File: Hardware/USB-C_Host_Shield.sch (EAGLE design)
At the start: 39 parts, among them J1 USB-C, J2 GPIN, J3 GPOUT, U1 ARDUINO_UNO_R3_SHIELDBASIC, U2 LM1117, U3 74HC4050, U5 MAX3421, U6 3.3V/150mA, Y1 12.0mhZ

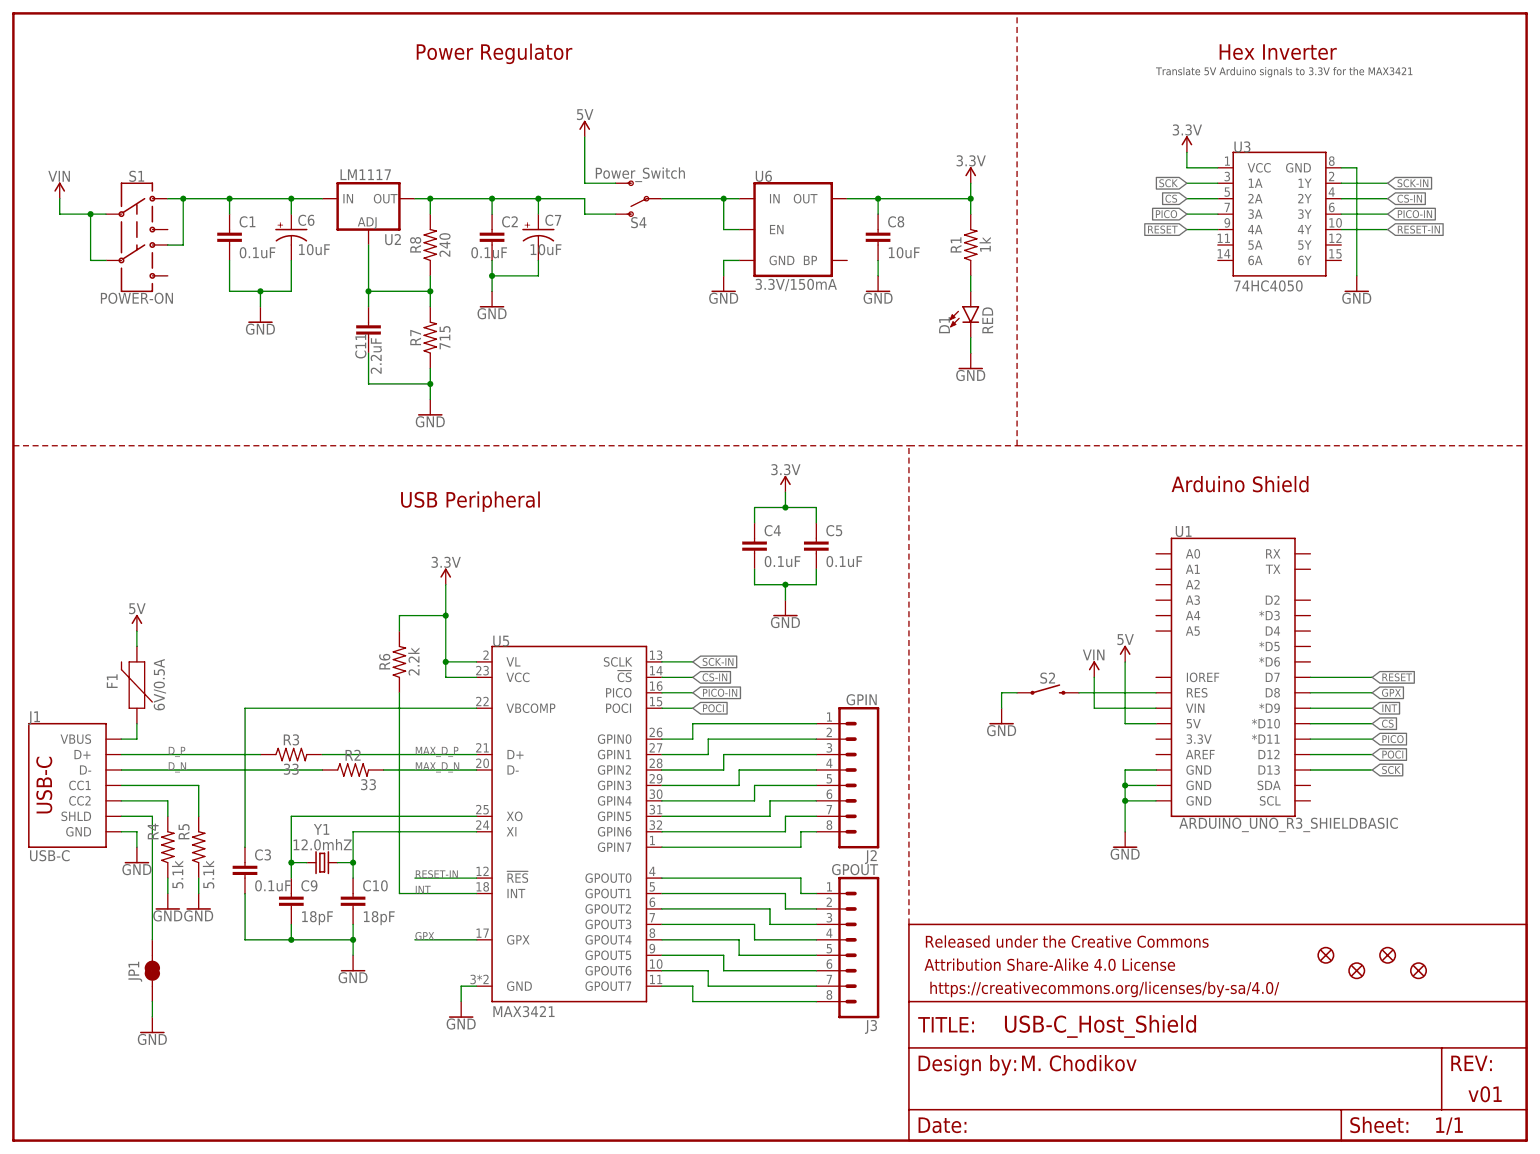
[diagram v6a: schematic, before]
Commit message: Updates from design review
Adjusted text in schematic to vector font, added pullup resistors to CC1 and CC2, changed power selection and power off section, added lines to silk screen GPIO pins
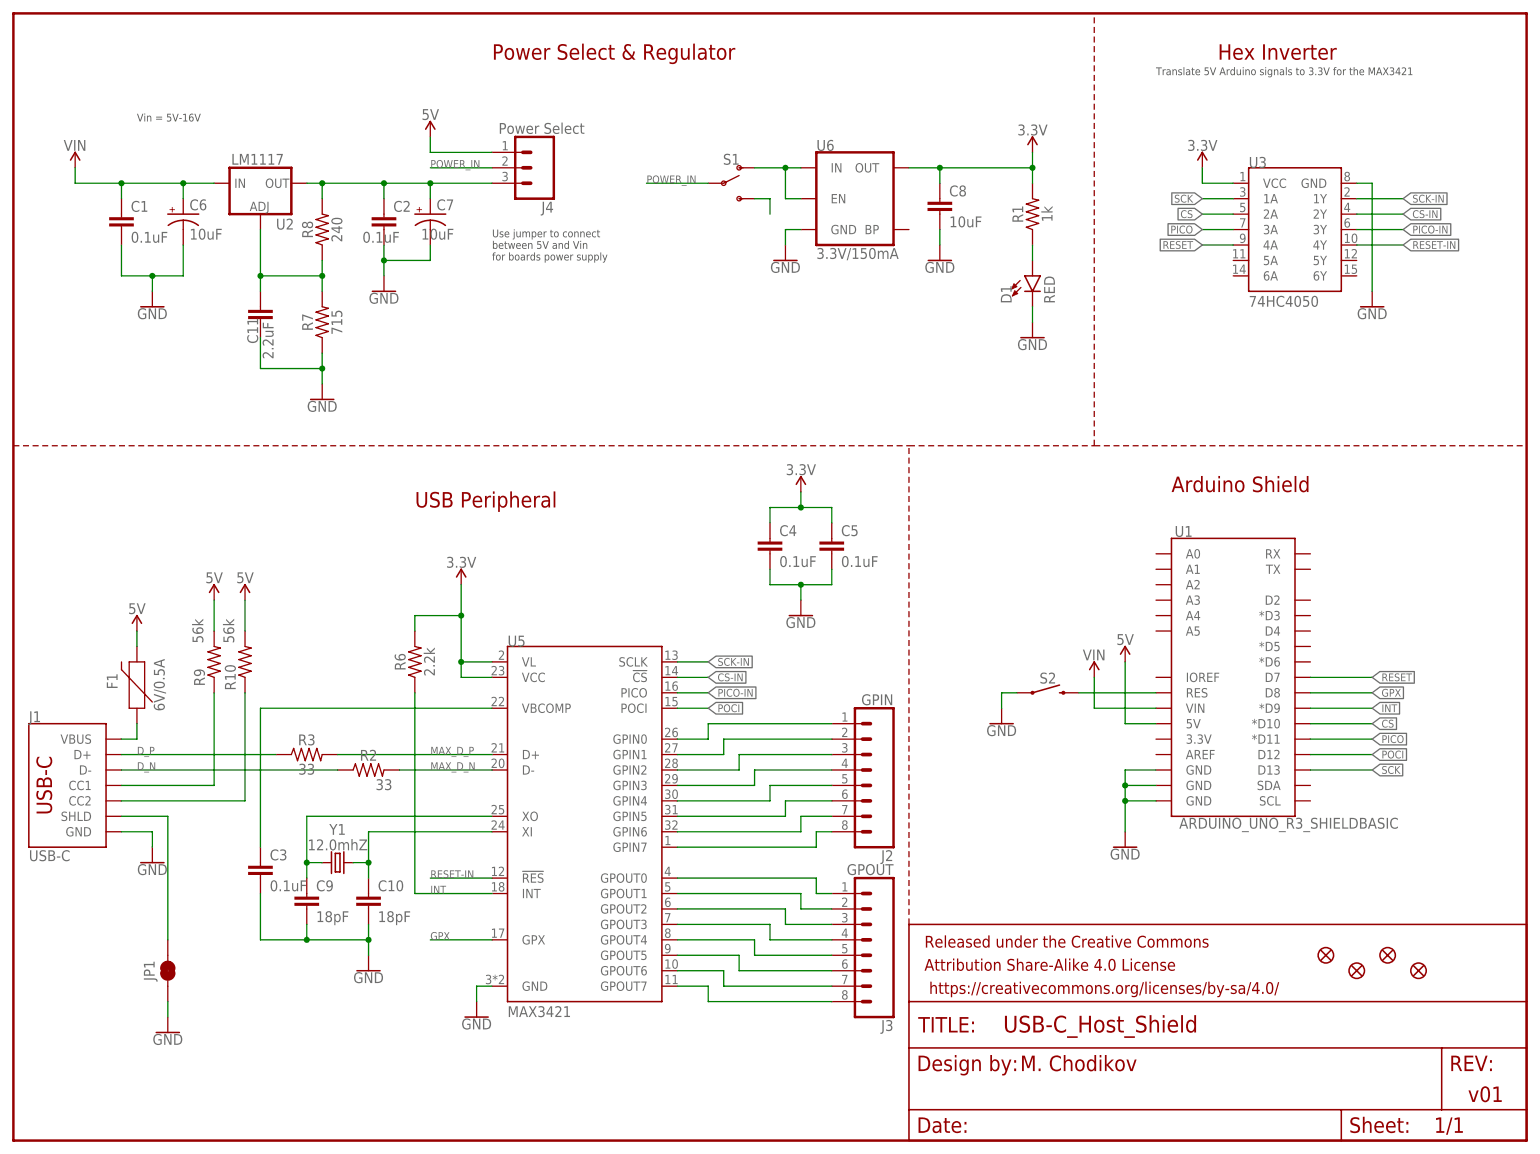
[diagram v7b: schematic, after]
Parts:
- removed R4, R5: 5.1k, SparkFun-Resistors:5.1KOHM5.1KOHM-0603-1/10W-1%
- removed S4: Power_Switch, SparkFun-Switches:SWITCH-SPDT-SMD-AYZ0202
- added J4: Power Select, SparkFun-Connectors:CONN_03
- added R10, R9: 56k, SparkFun-Resistors:56KOHM
- S1: value POWER-ON -> (none); device SparkFun-Switches:SWITCH-DPDT-SMD-AYZ0202 -> SparkFun-Switches:SWITCH-SPDT-SMD-AYZ0202
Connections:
- removed net N$5: S4.P, U6.EN, U6.IN
- new net POWER_IN: J4.2, S1.O, S1.P, U6.EN, U6.IN
- net 5V: now also J4.1, R10.2, R9.2; no longer S4.S
- net CC1: now also R9.1; no longer R5.2
- net CC2: now also R10.1; no longer R4.2
- net GND: no longer R4.1, R5.1
- net N$2: now also S1.S; no longer C1.1, C6.+, S1.3, S1.6, U2.IN
- net N$6: now also J4.3; no longer S4.O
- net VIN: now also C1.1, C6.+, U2.IN; no longer S1.2, S1.5
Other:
- note added: "Power Select & Regulator"
- note added: "Use jumper to connect between 5V and Vin for boards power supply"
- note added: "Vin = 5V-16V"
- note removed: "Power Regulator"
- moved on the sheet: C1, C10, C11, C2, C3, C4, C5, C6, C7, C8, C9, D1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

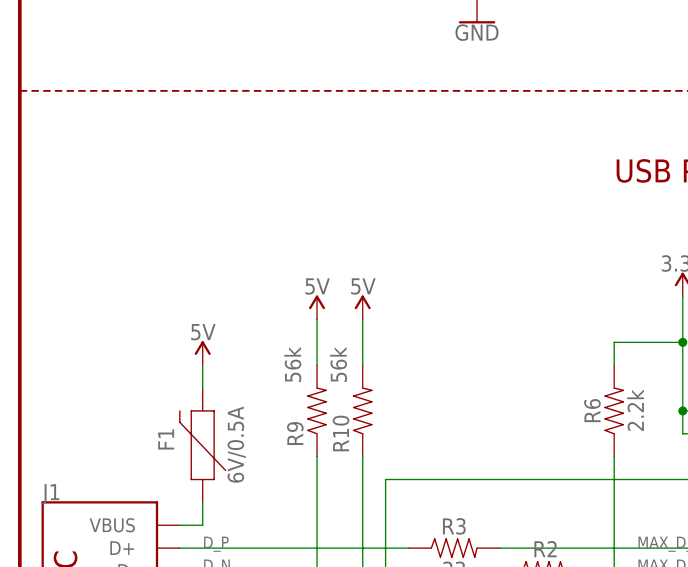
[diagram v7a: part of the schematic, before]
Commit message: Adjusted schematic with new changes for layout
Changed the main power schema for the USB-C port
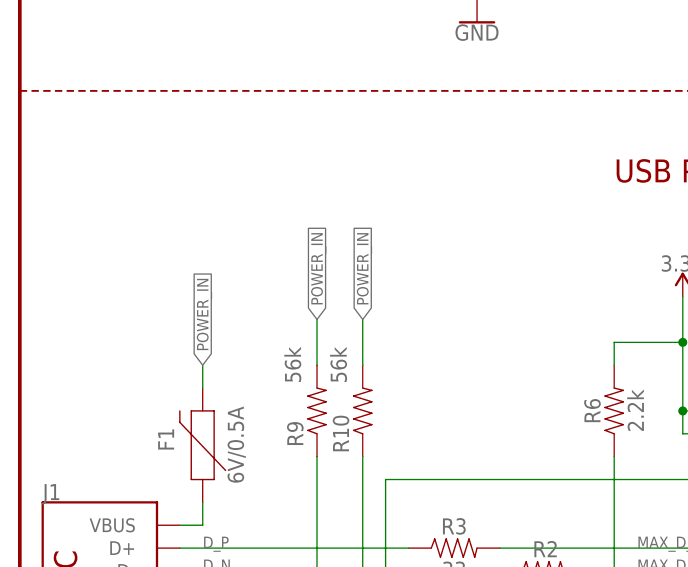
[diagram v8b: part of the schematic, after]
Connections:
- net 5V: no longer F1.2, R10.2, R9.2
- net POWER_IN: now also F1.2, R10.2, R9.2
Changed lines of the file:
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@@
 <part name="R2" library="SparkFun-Resistors" deviceset="33OHM" device="-0603-1/10W-1%" value="33"/>
 <part name="R3" library="SparkFun-Resistors" deviceset="33OHM" device="-0603-1/10W-1%" value="33"/>
-<part name="SUPPLY3" library="SparkFun-PowerSymbols" deviceset="5V" device=""/>
 <part name="GND8" library="SparkFun-PowerSymbols" deviceset="GND" device=""/>
 <part name="GND9" library="SparkFun-PowerSymbols" deviceset="GND" device=""/>
@@
 <part name="R9" library="SparkFun-Resistors" deviceset="56KOHM" device="" value="56k"/>
 <part name="R10" library="SparkFun-Resistors" deviceset="56KOHM" device="" value="56k"/>
-<part name="SUPPLY10" library="SparkFun-PowerSymbols" deviceset="5V" device=""/>
-<part name="SUPPLY11" library="SparkFun-PowerSymbols" deviceset="5V" device=""/>
 </parts>
 <sheets>
@@
 <attribute name="VALUE" x="48.26" y="61.976" size="1.778" layer="96" font="vector" align="top-center"/>
 </instance>
-<instance part="SUPPLY3" gate="G$1" x="20.32" y="83.82" smashed="yes">
-<attribute name="VALUE" x="20.32" y="86.614" size="1.778" layer="96" font="vector" align="bottom-center"/>
-</instance>
 <instance part="GND8" gate="1" x="22.86" y="45.72" smashed="yes">
 <attribute name="VALUE" x="22.86" y="45.466" size="1.778" layer="96" font="vector" align="top-center"/>
@@
 <attribute name="NAME" x="36.576" y="76.2" size="1.778" layer="95" font="vector" rot="R90" align="bottom-center"/>
 <attribute name="VALUE" x="34.544" y="83.82" size="1.778" layer="96" font="vector" rot="R90" align="top-center"/>
-</instance>
-<instance part="SUPPLY10" gate="G$1" x="33.02" y="88.9" smashed="yes">
-<attribute name="VALUE" x="33.02" y="91.694" size="1.778" layer="96" font="vector" align="bottom-center"/>
-</instance>
-<instance part="SUPPLY11" gate="G$1" x="38.1" y="88.9" smashed="yes">
-<attribute name="VALUE" x="38.1" y="91.694" size="1.778" layer="96" font="vector" align="bottom-center"/>
 </instance>
 </instances>
@@
 <net name="5V" class="0">
 <segment>
-<pinref part="F1" gate="F1" pin="2"/>
-<pinref part="SUPPLY3" gate="G$1" pin="5V"/>
-<wire x1="20.32" y1="81.28" x2="20.32" y2="83.82" width="0.1524" layer="91"/>
-</segment>
-<segment>
 <pinref part="U1" gate="G$1" pin="5V"/>
 <wire x1="187.96" y1="68.58" x2="182.88" y2="68.58" width="0.1524" layer="91"/>
@@
 <pinref part="J4" gate="J$1" pin="1"/>
 <wire x1="68.58" y1="162.56" x2="78.74" y2="162.56" width="0.1524" layer="91"/>
-</segment>
-<segment>
-<pinref part="R9" gate="G$1" pin="2"/>
-<wire x1="33.02" y1="83.82" x2="33.02" y2="88.9" width="0.1524" layer="91"/>
-<pinref part="SUPPLY10" gate="G$1" pin="5V"/>
-</segment>
-<segment>
-<pinref part="R10" gate="G$1" pin="2"/>
-<wire x1="38.1" y1="83.82" x2="38.1" y2="88.9" width="0.1524" layer="91"/>
-<pinref part="SUPPLY11" gate="G$1" pin="5V"/>
 </segment>
 </net>
@@
 <label x="104.14" y="157.48" size="1.27" layer="95" font="vector"/>
 </segment>
-</net>
+<segment>
+<pinref part="F1" gate="F1" pin="2"/>
+<wire x1="20.32" y1="81.28" x2="20.32" y2="83.82" width="0.1524" layer="91"/>
+<label x="20.32" y="83.82" size="1.27" layer="95" rot="R90" xref="yes"/>
+</segment>
+<segment>
+<pinref part="R9" gate="G$1" pin="2"/>
+<wire x1="33.02" y1="83.82" x2="33.02" y2="88.9" width="0.1524" layer="91"/>
+<label x="33.02" y="88.9" size="1.27" layer="95" rot="R90" xref="yes"/>
+</segment>
+<segment>
+<pinref part="R10" gate="G$1" pin="2"/>
+<wire x1="38.1" y1="83.82" x2="38.1" y2="88.9" width="0.1524" layer="91"/>
+<label x="38.1" y="88.9" size="1.27" layer="95" rot="R90" xref="yes"/>
+</segment>
+</net>
